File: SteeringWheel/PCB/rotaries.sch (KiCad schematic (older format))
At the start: 17 parts

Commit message: Steering Wheel Update
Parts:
- removed ScreenChg_RotarySwitch1: SW_Rotary6, symbol Switch:SW_Rotary6
- removed Uni_RotarySwitch1: SW_Rotary10, symbol Switch:SW_Rotary10
- added 1k16, 1k17, 1k18: 1k, Resistor_SMD:R_0805_2012Metric, symbol Device:R_Small
- added ScreenCHG1, UniCHG1: SR2512F-0110-19R0B-E9-N-W-159, PGR-06_Additional:Alpha_Taiwan-SR2512F-0110-19R0B-E9-N-W-159-MFG, symbol Alpha-SR2512F:SR2512F-0110-19R0B-E9-N-W-159
- 1k1, 1k10, 1k11, 1k12, 1k13, 1k14, 1k15, 1k2, 1k3, 1k4, 1k5, 1k6, 1k7, 1k8, 1k9: footprint (none) -> Resistor_SMD:R_0805_2012Metric
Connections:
- net labels removed: ROT_UNI
- wire segments 45 -> 58

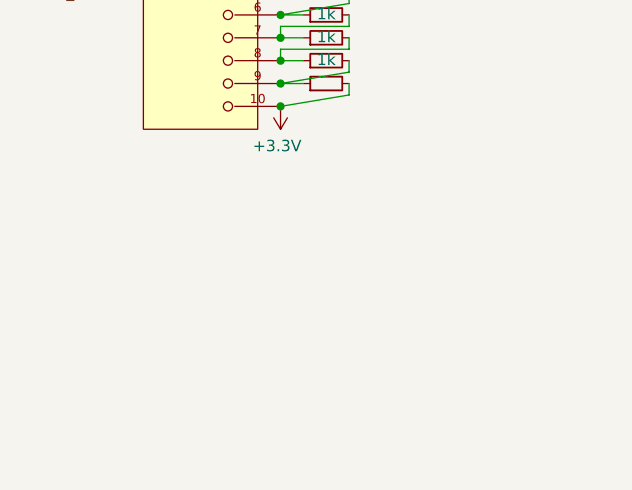
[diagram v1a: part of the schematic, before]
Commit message: New brd for steering wheel
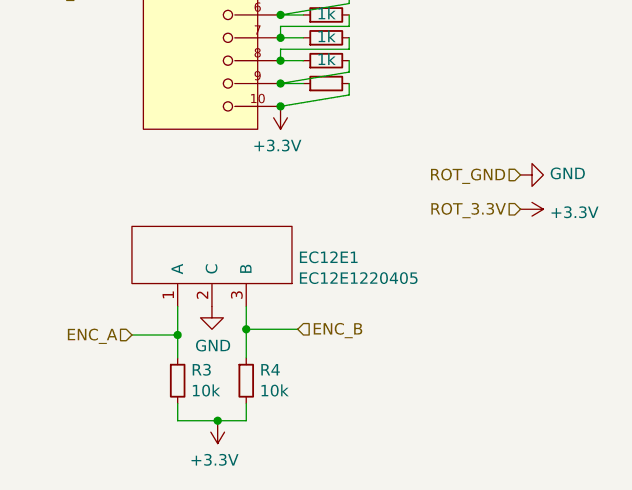
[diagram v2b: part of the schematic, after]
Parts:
- added EC12E1: EC12E1220405, PGR-06_Additional:EC12E1220405, symbol PGR-06_Wheel_Additional:EC12E1220405
- added R3, R4: 10k, Resistor_SMD:R_0805_2012Metric, symbol Device:R_Small
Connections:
- net +3V3: now also R3.2, R4.2
- net GND: now also EC12E1.2 (C)
- new net ENC_A: EC12E1.1 (A), R3.1
- new net ENC_B: EC12E1.3 (B), R4.1
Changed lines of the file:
@@
 $Descr A4 11693 8268
 encoding utf-8
-Sheet 3 3
+Sheet 2 3
 Title ""
 Date ""
@@
 $EndComp
 Connection ~ 2025 3025
+$Comp
+L PGR-06_Wheel_Additional:EC12E1220405 EC12E1
+U 1 1 61D02DB2
+P 1725 4400
+F 0 "EC12E1" H 2103 4213 50  0000 L CNN
+F 1 "EC12E1220405" H 2103 4122 50  0000 L CNN
+F 2 "PGR-06_Additional:EC12E1220405" H 1725 4400 50  0001 C CNN
+F 3 "" H 1725 4400 50  0001 C CNN
+	1    1725 4400
+	1    0    0    -1
+$EndComp
+$Comp
+L Device:R_Small R3
+U 1 1 61D02DB8
+P 1575 5125
+F 0 "R3" H 1634 5171 50  0000 L CNN
+F 1 "10k" H 1634 5080 50  0000 L CNN
+F 2 "Resistor_SMD:R_0805_2012Metric" H 1575 5125 50  0001 C CNN
+F 3 "~" H 1575 5125 50  0001 C CNN
+	1    1575 5125
+	1    0    0    -1
+$EndComp
+$Comp
+L Device:R_Small R4
+U 1 1 61D02DBE
+P 1875 5125
+F 0 "R4" H 1934 5171 50  0000 L CNN
+F 1 "10k" H 1934 5080 50  0000 L CNN
+F 2 "Resistor_SMD:R_0805_2012Metric" H 1875 5125 50  0001 C CNN
+F 3 "~" H 1875 5125 50  0001 C CNN
+	1    1875 5125
+	1    0    0    -1
+$EndComp
+$Comp
+L power:+3.3V #PWR0150
+U 1 1 61D02DC5
+P 1750 5300
+F 0 "#PWR0150" H 1750 5150 50  0001 C CNN
+F 1 "+3.3V" H 1765 5473 50  0000 C CNN
+F 2 "" H 1750 5300 50  0001 C CNN
+F 3 "" H 1750 5300 50  0001 C CNN
+	1    1750 5300
+	-1   0    0    1
+$EndComp
+Wire Wire Line
+	1575 5225 1575 5300
+Wire Wire Line
+	1875 5225 1875 5300
+Wire Wire Line
+	1575 5300 1750 5300
+Connection ~ 1750 5300
+Wire Wire Line
+	1750 5300 1875 5300
+$Comp
+L power:GND #PWR0151
+U 1 1 61D02DD0
+P 1725 4800
+F 0 "#PWR0151" H 1725 4550 50  0001 C CNN
+F 1 "GND" H 1730 4627 50  0000 C CNN
+F 2 "" H 1725 4800 50  0001 C CNN
+F 3 "" H 1725 4800 50  0001 C CNN
+	1    1725 4800
+	1    0    0    -1
+$EndComp
+Text HLabel 1375 4925 0    50   Input ~ 0
+ENC_A
+Text HLabel 2100 4900 2    50   Input ~ 0
+ENC_B
+Wire Wire Line
+	1875 4800 1875 4900
+Wire Wire Line
+	1575 4800 1575 4925
+Wire Wire Line
+	1375 4925 1575 4925
+Connection ~ 1575 4925
+Wire Wire Line
+	1575 4925 1575 5025
+Wire Wire Line
+	2100 4900 1875 4900
+Connection ~ 1875 4900
+Wire Wire Line
+	1875 4900 1875 5025
+Text HLabel 3075 4225 0    50   Input ~ 0
+ROT_GND
+Text HLabel 3075 4375 0    50   Input ~ 0
+ROT_3.3V
+$Comp
+L power:GND #PWR0148
+U 1 1 61DDD949
+P 3075 4225
+F 0 "#PWR0148" H 3075 3975 50  0001 C CNN
+F 1 "GND" V 3080 4097 50  0000 R CNN
+F 2 "" H 3075 4225 50  0001 C CNN
+F 3 "" H 3075 4225 50  0001 C CNN
+	1    3075 4225
+	0    -1   -1   0
+$EndComp
+$Comp
+L power:+3.3V #PWR0149
+U 1 1 61DDE0C7
+P 3075 4375
+F 0 "#PWR0149" H 3075 4225 50  0001 C CNN
+F 1 "+3.3V" V 3090 4503 50  0000 L CNN
+F 2 "" H 3075 4375 50  0001 C CNN
+F 3 "" H 3075 4375 50  0001 C CNN
+	1    3075 4375
+	0    1    1    0
+$EndComp
 $EndSCHEMATC

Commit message: Steering Wheel Update
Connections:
- net ROT_SCR: no longer UniCHG1.11 (Pole)
- new net ROT_UNI: UniCHG1.11 (Pole)
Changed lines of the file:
@@
 $EndComp
 Connection ~ 2075 1425
-Text HLabel 1325 3425 0    50   Input ~ 0
-ROT_SCR
 $Comp
 L Device:R_Small 1k?
@@
 Wire Wire Line
 	2125 3825 2025 3825
+Wire Wire Line
+	2325 3675 2025 3675
+Wire Wire Line
+	2025 3675 2025 3725
+Wire Wire Line
+	2125 3725 2025 3725
+$Comp
+L Device:R_Small 1k?
+U 1 1 61BB2C75
+P 2225 3725
+AR Path="/61BB2C75" Ref="1k?"  Part="1"
+AR Path="/619ACF8C/61BB2C75" Ref="1k8"  Part="1"
+F 0 "1k8" V 2421 3725 50  0001 C CNN
+F 1 "1k" V 2329 3725 50  0000 C CNN
+F 2 "Resistor_SMD:R_0805_2012Metric" H 2225 3725 50  0001 C CNN
+F 3 "~" H 2225 3725 50  0001 C CNN
+	1    2225 3725
+	0    -1   -1   0
+$EndComp
+Wire Wire Line
+	2325 3525 2325 3575
+Wire Wire Line
+	2325 3575 2025 3575
+Wire Wire Line
+	2025 3575 2025 3625
+$Comp
+L power:+3.3V #PWR0118
+U 1 1 61BB2C7F
+P 2025 3925
+F 0 "#PWR0118" H 2025 3775 50  0001 C CNN
+F 1 "+3.3V" H 2040 4098 50  0000 C CNN
+F 2 "" H 2025 3925 50  0001 C CNN
+F 3 "" H 2025 3925 50  0001 C CNN
+	1    2025 3925
+	-1   0    0    1
+$EndComp
+$Comp
+L power:GND #PWR0119
+U 1 1 61BB2C86
+P 2025 3025
+F 0 "#PWR0119" H 2025 2775 50  0001 C CNN
+F 1 "GND" H 2030 2852 50  0000 C CNN
+F 2 "" H 2025 3025 50  0001 C CNN
+F 3 "" H 2025 3025 50  0001 C CNN
+	1    2025 3025
+	-1   0    0    1
+$EndComp
+$Comp
+L PGR-06_Wheel_Additional:EC12E1220405 EC12E1
+U 1 1 61D02DB2
+P 1725 4400
+F 0 "EC12E1" H 2103 4213 50  0000 L CNN
+F 1 "EC12E1220405" H 2103 4122 50  0000 L CNN
+F 2 "PGR-06_Additional:EC12E1220405" H 1725 4400 50  0001 C CNN
+F 3 "" H 1725 4400 50  0001 C CNN
+	1    1725 4400
+	1    0    0    -1
+$EndComp
+$Comp
+L Device:R_Small R3
+U 1 1 61D02DB8
+P 1575 5125
+F 0 "R3" H 1634 5171 50  0000 L CNN
+F 1 "10k" H 1634 5080 50  0000 L CNN
+F 2 "Resistor_SMD:R_0805_2012Metric" H 1575 5125 50  0001 C CNN
+F 3 "~" H 1575 5125 50  0001 C CNN
+	1    1575 5125
+	1    0    0    -1
+$EndComp
+$Comp
+L Device:R_Small R4
+U 1 1 61D02DBE
+P 1875 5125
+F 0 "R4" H 1934 5171 50  0000 L CNN
+F 1 "10k" H 1934 5080 50  0000 L CNN
+F 2 "Resistor_SMD:R_0805_2012Metric" H 1875 5125 50  0001 C CNN
+F 3 "~" H 1875 5125 50  0001 C CNN
+	1    1875 5125
+	1    0    0    -1
+$EndComp
+$Comp
+L power:+3.3V #PWR0150
+U 1 1 61D02DC5
+P 1750 5300
+F 0 "#PWR0150" H 1750 5150 50  0001 C CNN
+F 1 "+3.3V" H 1765 5473 50  0000 C CNN
+F 2 "" H 1750 5300 50  0001 C CNN
+F 3 "" H 1750 5300 50  0001 C CNN
+	1    1750 5300
+	-1   0    0    1
+$EndComp
+Wire Wire Line
+	1575 5225 1575 5300
+Wire Wire Line
+	1875 5225 1875 5300
+Wire Wire Line
+	1575 5300 1750 5300
+Connection ~ 1750 5300
+Wire Wire Line
+	1750 5300 1875 5300
+$Comp
+L power:GND #PWR0151
+U 1 1 61D02DD0
+P 1725 4800
+F 0 "#PWR0151" H 1725 4550 50  0001 C CNN
+F 1 "GND" H 1730 4627 50  0000 C CNN
+F 2 "" H 1725 4800 50  0001 C CNN
+F 3 "" H 1725 4800 50  0001 C CNN
+	1    1725 4800
+	1    0    0    -1
+$EndComp
+Text HLabel 1375 4925 0    50   Input ~ 0
+ENC_A
+Text HLabel 2100 4900 2    50   Input ~ 0
+ENC_B
+Wire Wire Line
+	1875 4800 1875 4900
+Wire Wire Line
+	1575 4800 1575 4925
+Wire Wire Line
+	1375 4925 1575 4925
+Connection ~ 1575 4925
+Wire Wire Line
+	1575 4925 1575 5025
+Wire Wire Line
+	2100 4900 1875 4900
+Connection ~ 1875 4900
+Wire Wire Line
+	1875 4900 1875 5025
+Text HLabel 3075 4225 0    50   Input ~ 0
+ROT_GND
+Text HLabel 3075 4375 0    50   Input ~ 0
+ROT_3.3V
+$Comp
+L power:GND #PWR0148
+U 1 1 61DDD949
+P 3075 4225
+F 0 "#PWR0148" H 3075 3975 50  0001 C CNN
+F 1 "GND" V 3080 4097 50  0000 R CNN
+F 2 "" H 3075 4225 50  0001 C CNN
+F 3 "" H 3075 4225 50  0001 C CNN
+	1    3075 4225
+	0    -1   -1   0
+$EndComp
+$Comp
+L power:+3.3V #PWR0149
+U 1 1 61DDE0C7
+P 3075 4375
+F 0 "#PWR0149" H 3075 4225 50  0001 C CNN
+F 1 "+3.3V" V 3090 4503 50  0000 L CNN
+F 2 "" H 3075 4375 50  0001 C CNN
+F 3 "" H 3075 4375 50  0001 C CNN
+	1    3075 4375
+	0    1    1    0
+$EndComp
+Connection ~ 2025 3025
+Connection ~ 2025 3925
+Connection ~ 2025 3625
+Connection ~ 2025 3725
+Connection ~ 2025 3125
+Connection ~ 2025 3225
+Connection ~ 2025 3325
+Connection ~ 2025 3425
+Connection ~ 2025 3525
 Connection ~ 2025 3825
-Connection ~ 2025 3525
-Connection ~ 2025 3425
-Connection ~ 2025 3325
-Connection ~ 2025 3225
-Connection ~ 2025 3125
 $Comp
 L Alpha-SR2512F:SR2512F-0110-19R0B-E9-N-W-159 UniCHG1
@@
 	1    0    0    -1
 $EndComp
-Wire Wire Line
-	2325 3675 2025 3675
-Connection ~ 2025 3725
-Wire Wire Line
-	2025 3675 2025 3725
-Wire Wire Line
-	2125 3725 2025 3725
-$Comp
-L Device:R_Small 1k?
-U 1 1 61BB2C75
-P 2225 3725
-AR Path="/61BB2C75" Ref="1k?"  Part="1"
-AR Path="/619ACF8C/61BB2C75" Ref="1k8"  Part="1"
-F 0 "1k8" V 2421 3725 50  0001 C CNN
-F 1 "1k" V 2329 3725 50  0000 C CNN
-F 2 "Resistor_SMD:R_0805_2012Metric" H 2225 3725 50  0001 C CNN
-F 3 "~" H 2225 3725 50  0001 C CNN
-	1    2225 3725
-	0    -1   -1   0
-$EndComp
-Wire Wire Line
-	2325 3525 2325 3575
-Wire Wire Line
-	2325 3575 2025 3575
-Wire Wire Line
-	2025 3575 2025 3625
-Connection ~ 2025 3625
-$Comp
-L power:+3.3V #PWR0118
-U 1 1 61BB2C7F
-P 2025 3925
-F 0 "#PWR0118" H 2025 3775 50  0001 C CNN
-F 1 "+3.3V" H 2040 4098 50  0000 C CNN
-F 2 "" H 2025 3925 50  0001 C CNN
-F 3 "" H 2025 3925 50  0001 C CNN
-	1    2025 3925
-	-1   0    0    1
-$EndComp
-Connection ~ 2025 3925
-$Comp
-L power:GND #PWR0119
-U 1 1 61BB2C86
-P 2025 3025
-F 0 "#PWR0119" H 2025 2775 50  0001 C CNN
-F 1 "GND" H 2030 2852 50  0000 C CNN
-F 2 "" H 2025 3025 50  0001 C CNN
-F 3 "" H 2025 3025 50  0001 C CNN
-	1    2025 3025
-	-1   0    0    1
-$EndComp
-Connection ~ 2025 3025
-$Comp
-L PGR-06_Wheel_Additional:EC12E1220405 EC12E1
-U 1 1 61D02DB2
-P 1725 4400
-F 0 "EC12E1" H 2103 4213 50  0000 L CNN
-F 1 "EC12E1220405" H 2103 4122 50  0000 L CNN
-F 2 "PGR-06_Additional:EC12E1220405" H 1725 4400 50  0001 C CNN
-F 3 "" H 1725 4400 50  0001 C CNN
-	1    1725 4400
-	1    0    0    -1
-$EndComp
-$Comp
-L Device:R_Small R3
-U 1 1 61D02DB8
-P 1575 5125
-F 0 "R3" H 1634 5171 50  0000 L CNN
-F 1 "10k" H 1634 5080 50  0000 L CNN
-F 2 "Resistor_SMD:R_0805_2012Metric" H 1575 5125 50  0001 C CNN
-F 3 "~" H 1575 5125 50  0001 C CNN
-	1    1575 5125
-	1    0    0    -1
-$EndComp
-$Comp
-L Device:R_Small R4
-U 1 1 61D02DBE
-P 1875 5125
-F 0 "R4" H 1934 5171 50  0000 L CNN
-F 1 "10k" H 1934 5080 50  0000 L CNN
-F 2 "Resistor_SMD:R_0805_2012Metric" H 1875 5125 50  0001 C CNN
-F 3 "~" H 1875 5125 50  0001 C CNN
-	1    1875 5125
-	1    0    0    -1
-$EndComp
-$Comp
-L power:+3.3V #PWR0150
-U 1 1 61D02DC5
-P 1750 5300
-F 0 "#PWR0150" H 1750 5150 50  0001 C CNN
-F 1 "+3.3V" H 1765 5473 50  0000 C CNN
-F 2 "" H 1750 5300 50  0001 C CNN
-F 3 "" H 1750 5300 50  0001 C CNN
-	1    1750 5300
-	-1   0    0    1
-$EndComp
-Wire Wire Line
-	1575 5225 1575 5300
-Wire Wire Line
-	1875 5225 1875 5300
-Wire Wire Line
-	1575 5300 1750 5300
-Connection ~ 1750 5300
-Wire Wire Line
-	1750 5300 1875 5300
-$Comp
-L power:GND #PWR0151
-U 1 1 61D02DD0
-P 1725 4800
-F 0 "#PWR0151" H 1725 4550 50  0001 C CNN
-F 1 "GND" H 1730 4627 50  0000 C CNN
-F 2 "" H 1725 4800 50  0001 C CNN
-F 3 "" H 1725 4800 50  0001 C CNN
-	1    1725 4800
-	1    0    0    -1
-$EndComp
-Text HLabel 1375 4925 0    50   Input ~ 0
-ENC_A
-Text HLabel 2100 4900 2    50   Input ~ 0
-ENC_B
-Wire Wire Line
-	1875 4800 1875 4900
-Wire Wire Line
-	1575 4800 1575 4925
-Wire Wire Line
-	1375 4925 1575 4925
-Connection ~ 1575 4925
-Wire Wire Line
-	1575 4925 1575 5025
-Wire Wire Line
-	2100 4900 1875 4900
-Connection ~ 1875 4900
-Wire Wire Line
-	1875 4900 1875 5025
-Text HLabel 3075 4225 0    50   Input ~ 0
-ROT_GND
-Text HLabel 3075 4375 0    50   Input ~ 0
-ROT_3.3V
-$Comp
-L power:GND #PWR0148
-U 1 1 61DDD949
-P 3075 4225
-F 0 "#PWR0148" H 3075 3975 50  0001 C CNN
-F 1 "GND" V 3080 4097 50  0000 R CNN
-F 2 "" H 3075 4225 50  0001 C CNN
-F 3 "" H 3075 4225 50  0001 C CNN
-	1    3075 4225
-	0    -1   -1   0
-$EndComp
-$Comp
-L power:+3.3V #PWR0149
-U 1 1 61DDE0C7
-P 3075 4375
-F 0 "#PWR0149" H 3075 4225 50  0001 C CNN
-F 1 "+3.3V" V 3090 4503 50  0000 L CNN
-F 2 "" H 3075 4375 50  0001 C CNN
-F 3 "" H 3075 4375 50  0001 C CNN
-	1    3075 4375
-	0    1    1    0
-$EndComp
+Text HLabel 1325 3425 0    50   Input ~ 0
+ROT_UNI
 $EndSCHEMATC
